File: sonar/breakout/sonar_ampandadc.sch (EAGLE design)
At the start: 19 parts

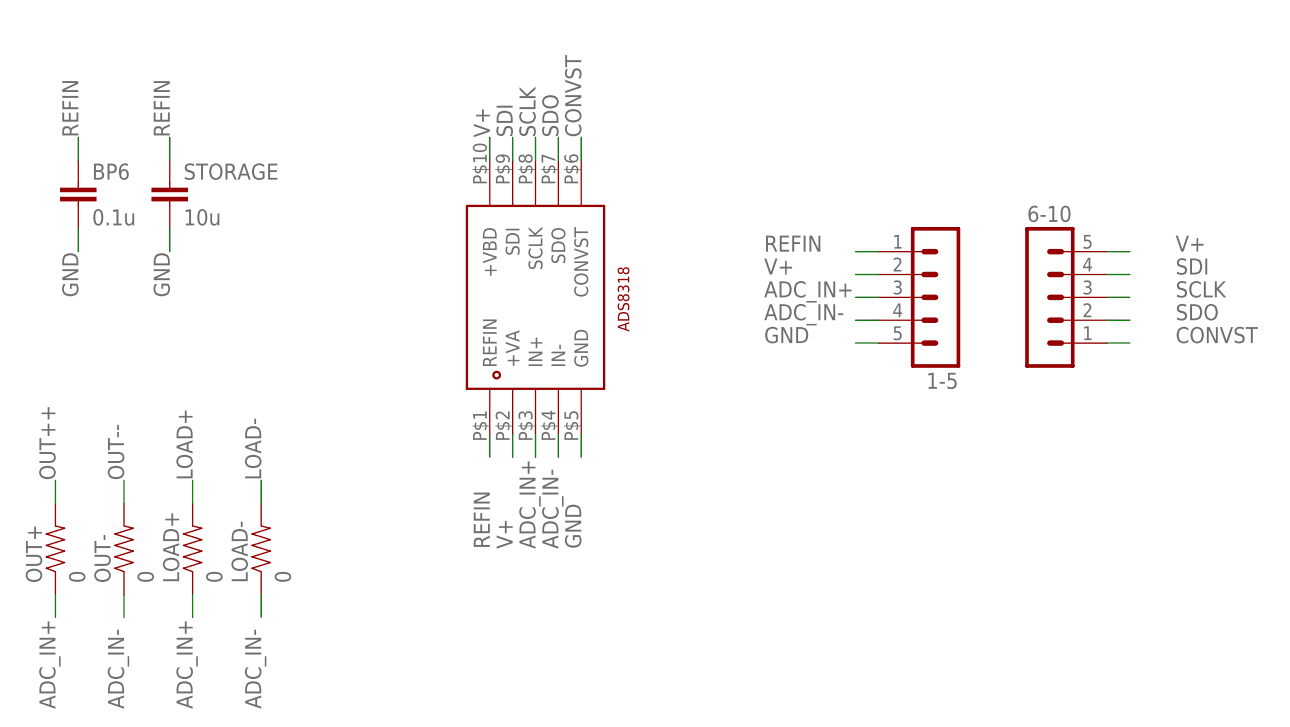
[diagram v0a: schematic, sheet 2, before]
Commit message: Made requested changes. When ordering be sure to tell them that I added a VSCORE layer in the middle of the board
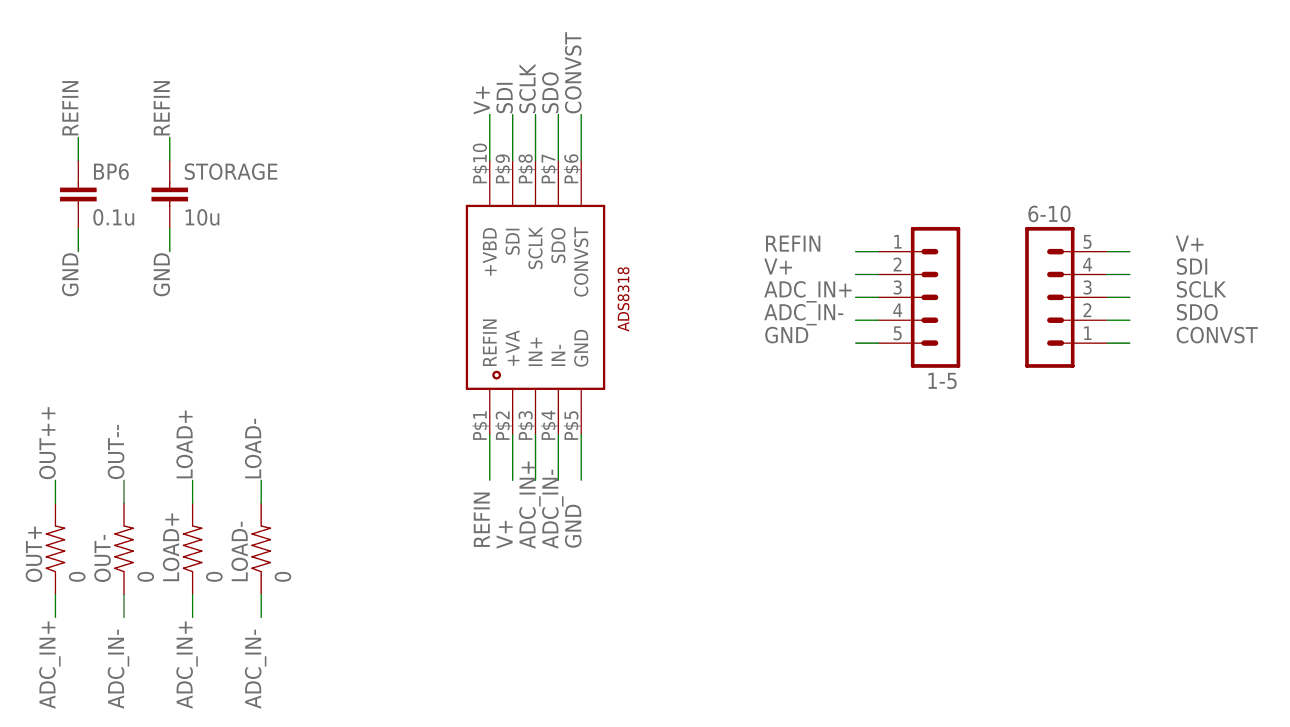
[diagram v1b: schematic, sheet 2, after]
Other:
- note added: "Analog to Digital Converter Breakout Board"
- note added: "Differential Variable Gain Amplifier Breakout Board"
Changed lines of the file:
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@@
 <wire x1="-86.36" y1="-45.72" x2="-86.36" y2="-12.7" width="0.1524" layer="98" style="longdash"/>
 <text x="-78.74" y="-10.16" size="1.778" layer="98">Set Output Common Mode</text>
+<text x="-119.38" y="27.94" size="5.08" layer="98">Differential Variable Gain Amplifier Breakout Board</text>
 </plain>
 <instances>
@@
 <text x="-14.986" y="23.876" size="1.778" layer="98">ADC input options</text>
 <text x="-15.24" y="59.436" size="1.778" layer="98">ADC reference caps</text>
+<text x="-12.7" y="66.04" size="5.08" layer="98">Analog to Digital Converter Breakout Board</text>
 </plain>
 <instances>
@@
 <segment>
 <pinref part="U$2" gate="G$1" pin="+VA"/>
-<wire x1="40.64" y1="15.24" x2="40.64" y2="12.7" width="0.1524" layer="91"/>
 <label x="40.64" y="2.54" size="1.778" layer="95" rot="R90"/>
+<wire x1="40.64" y1="15.24" x2="40.64" y2="10.16" width="0.1524" layer="91"/>
 </segment>
 <segment>
 <pinref part="U$2" gate="G$1" pin="+VBD"/>
-<wire x1="38.1" y1="45.72" x2="38.1" y2="48.26" width="0.1524" layer="91"/>
-<label x="38.1" y="48.26" size="1.778" layer="95" rot="R90"/>
+<wire x1="38.1" y1="45.72" x2="38.1" y2="50.8" width="0.1524" layer="91"/>
+<label x="38.1" y="50.8" size="1.778" layer="95" rot="R90"/>
 </segment>
 <segment>
@@
 <segment>
 <pinref part="U$2" gate="G$1" pin="CONVST"/>
-<wire x1="48.26" y1="45.72" x2="48.26" y2="48.26" width="0.1524" layer="91"/>
-<label x="48.26" y="48.26" size="1.778" layer="95" rot="R90"/>
+<wire x1="48.26" y1="45.72" x2="48.26" y2="50.8" width="0.1524" layer="91"/>
+<label x="48.26" y="50.8" size="1.778" layer="95" rot="R90"/>
 </segment>
 <segment>
@@
 <segment>
 <pinref part="U$2" gate="G$1" pin="SDO"/>
-<wire x1="45.72" y1="45.72" x2="45.72" y2="48.26" width="0.1524" layer="91"/>
-<label x="45.72" y="48.26" size="1.778" layer="95" rot="R90"/>
+<wire x1="45.72" y1="45.72" x2="45.72" y2="50.8" width="0.1524" layer="91"/>
+<label x="45.72" y="50.8" size="1.778" layer="95" rot="R90"/>
 </segment>
 <segment>
@@
 <segment>
 <pinref part="U$2" gate="G$1" pin="SCLK"/>
-<wire x1="43.18" y1="45.72" x2="43.18" y2="48.26" width="0.1524" layer="91"/>
-<label x="43.18" y="48.26" size="1.778" layer="95" rot="R90"/>
+<wire x1="43.18" y1="45.72" x2="43.18" y2="50.8" width="0.1524" layer="91"/>
+<label x="43.18" y="50.8" size="1.778" layer="95" rot="R90"/>
 </segment>
 <segment>
@@
 <segment>
 <pinref part="U$2" gate="G$1" pin="SDI"/>
-<wire x1="40.64" y1="45.72" x2="40.64" y2="48.26" width="0.1524" layer="91"/>
-<label x="40.64" y="48.26" size="1.778" layer="95" rot="R90"/>
+<wire x1="40.64" y1="45.72" x2="40.64" y2="50.8" width="0.1524" layer="91"/>
+<label x="40.64" y="50.8" size="1.778" layer="95" rot="R90"/>
 </segment>
 <segment>
@@
 <segment>
 <pinref part="U$2" gate="G$1" pin="GND"/>
-<wire x1="48.26" y1="15.24" x2="48.26" y2="12.7" width="0.1524" layer="91"/>
 <label x="48.26" y="2.54" size="1.778" layer="95" rot="R90"/>
+<wire x1="48.26" y1="15.24" x2="48.26" y2="10.16" width="0.1524" layer="91"/>
 </segment>
 <segment>
@@
 <segment>
 <pinref part="U$2" gate="G$1" pin="REFIN"/>
-<wire x1="38.1" y1="15.24" x2="38.1" y2="12.7" width="0.1524" layer="91"/>
 <label x="38.1" y="2.54" size="1.778" layer="95" rot="R90"/>
+<wire x1="38.1" y1="15.24" x2="38.1" y2="10.16" width="0.1524" layer="91"/>
 </segment>
 <segment>
@@
 <segment>
 <pinref part="U$2" gate="G$1" pin="IN+"/>
-<wire x1="43.18" y1="15.24" x2="43.18" y2="12.7" width="0.1524" layer="91"/>
 <label x="43.18" y="2.54" size="1.778" layer="95" rot="R90"/>
+<wire x1="43.18" y1="15.24" x2="43.18" y2="10.16" width="0.1524" layer="91"/>
 </segment>
 <segment>
@@
 <segment>
 <pinref part="U$2" gate="G$1" pin="IN-"/>
-<wire x1="45.72" y1="15.24" x2="45.72" y2="12.7" width="0.1524" layer="91"/>
 <label x="45.72" y="2.54" size="1.778" layer="95" rot="R90"/>
-</segment>
-<segment>
+<wire x1="45.72" y1="15.24" x2="45.72" y2="10.16" width="0.1524" layer="91"/>
+</segment>
+<segment>
